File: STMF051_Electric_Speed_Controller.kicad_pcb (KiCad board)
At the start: 4 copper layers, 46 x 47 mm, 166 parts, among them J1 Conn_01x03_Pin, J2 Conn_01x03_Pin, J3 Conn_01x03_Pin, J4 Conn_01x03_Pin, J5 Conn_01x03_Pin, J6 Conn_01x03_Pin, Q1 TPH3R704PL,L1Q, Q10 TPH3R704PL,L1Q, Q11 TPH3R704PL,L1Q, Q12 TPH3R704PL,L1Q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

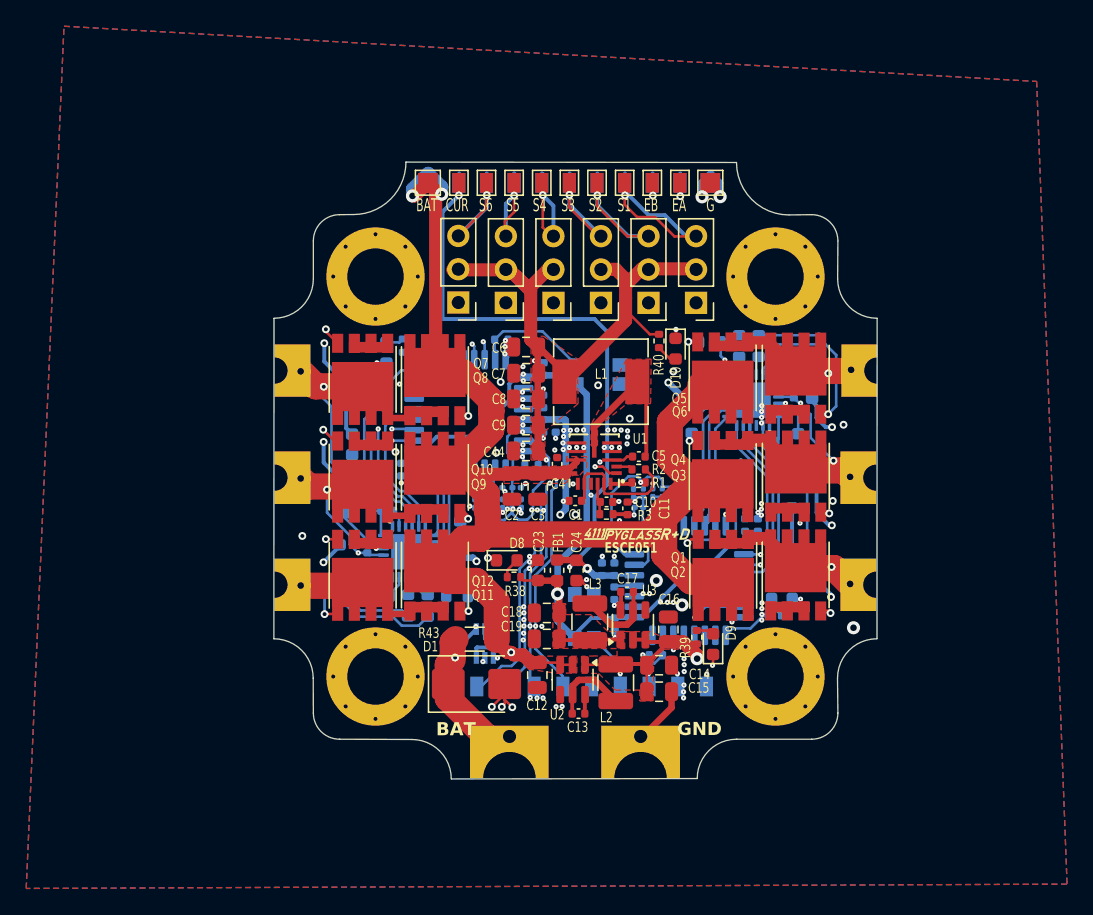
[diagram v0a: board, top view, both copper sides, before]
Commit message: remove blind vias
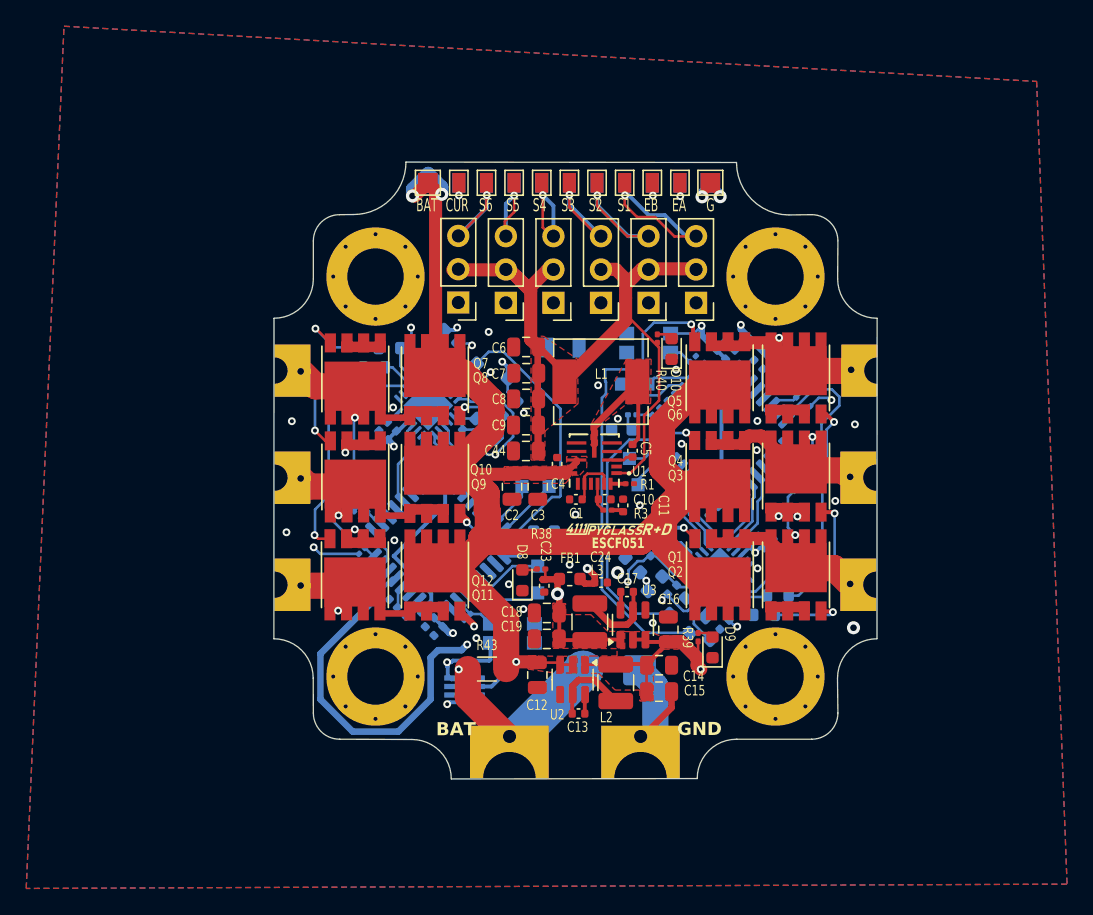
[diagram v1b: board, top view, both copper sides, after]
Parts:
- removed the G*** at (100.7, 91.0)
- removed R2: 22k0, Resistor_SMD:R_0402_1005Metric
- C23, C24: footprint Capacitor_SMD:C_0603_1608Metric -> Capacitor_SMD:C_0402_1005Metric
- D1: moved to B.Cu
- R1, R21, R22, R3, R38, R39, R4, R40, R41, R42, R5: footprint Resistor_SMD:R_0402_1005Metric -> ProjectLibrary:R_0201_0603Metric
- TP10, TP11, TP3, TP4, TP8, TP9: footprint ProjectLibrary:TestPoint_Pad_1.0x1.5mm -> TestPoint:TestPoint_Pad_1.0x1.0mm
- TP5: renamed from TP6; footprint ProjectLibrary:TestPoint_Pad_1.0x1.5mm -> TestPoint:TestPoint_Pad_1.0x1.0mm
- TP6: renamed from TP7; footprint ProjectLibrary:TestPoint_Pad_1.0x1.5mm -> TestPoint:TestPoint_Pad_1.0x1.0mm
- moved TP7 26.9 mm to (97.8, 91.2)
- moved TP12 25.8 mm to (100.3, 91.2)
- moved TP4 23.2 mm to (105.5, 94.0), turned to 0 degrees
- moved TP3 23.2 mm to (103.5, 94.0), turned to 0 degrees
- moved R5 22.8 mm to (109.0, 92.0), turned to 45 degrees
- moved C21 22.4 mm to (111.8, 91.7), turned to 45 degrees
- moved R19 21.6 mm to (109.3, 112.3), turned to 45 degrees
- moved D4 21.5 mm to (109.7, 114.0), turned to -135 degrees
- moved SW1 21.4 mm to (105.6, 90.8), turned to 180 degrees
- moved R21 21.3 mm to (91.8, 111.7), turned to -135 degrees
- moved SW2 20.8 mm to (95.2, 113.0)
- moved C25 20.6 mm to (114.0, 92.5), turned to -45 degrees
- moved C27 20.4 mm to (115.9, 93.1), turned to -45 degrees
- moved R15 19.8 mm to (114.4, 111.5)
- moved C32 19.4 mm to (111.4, 112.3), turned to 45 degrees
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- renumbered TP5 to TP7
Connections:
- net Net-(Q1-Pad4) renamed /FET Driver/HOGate01_A
- net Net-(Q10-Pad4) renamed /FET Driver/LOGate02_B
- net Net-(Q11-Pad4) renamed /FET Driver/HOGate03_B
- net Net-(Q12-Pad4) renamed /FET Driver/LOGate03_B
- net Net-(Q2-Pad4) renamed /FET Driver/LOGate01_A
- net Net-(Q3-Pad4) renamed /FET Driver/HOGate02_A
- net Net-(Q4-Pad4) renamed /FET Driver/LOGate02_A
- net Net-(Q5-Pad4) renamed /FET Driver/HOGate03_A
- net Net-(Q6-Pad4) renamed /FET Driver/LOGate03_A
- net Net-(Q7-Pad4) renamed /FET Driver/HOGate01_B
- net Net-(Q8-Pad4) renamed /FET Driver/LOGate01_B
- net Net-(Q9-Pad4) renamed /FET Driver/HOGate02_B
- SW1 pad 1: /MCU/BOOT0_A -> +3.3V
- SW1 pad 2: +3.3V -> /MCU/BOOT0_A
- U1 pad 2: Net-(U1-*RESET) -> unconnected-(U1-*RESET-Pad2)
- U4 pad 18: HIN1_A -> HIN3_A
- U4 pad 20: HIN3_A -> HIN1_A
- U6 pad 18: HIN1_B -> HIN3_B
- U6 pad 20: HIN3_B -> HIN1_B
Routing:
- net +5V: track 187.2 -> 122.6 mm, vias 9 -> 6
- net +3.3VA: track 22.1 -> 77.0 mm, vias 2 -> 3
- net /FET Driver/HOGate03_A: track 1.81 -> 36.3 mm
- net /FET Driver/HOGate03_B: track 1.82 -> 30.1 mm, vias 1 -> 2
- net RX1_B: track 32.2 -> 5.90 mm, vias 2 -> 0
- net SWDIO_B: track 29.5 -> 3.65 mm, vias 2 -> 0
- net GND: track 44.2 -> 18.7 mm, vias 147 -> 30
- net TX1_B: track 31.3 -> 5.87 mm, vias 2 -> 0
- net SWCLK_B: track 29.8 -> 4.93 mm, vias 2 -> 0
- net PHASE1_A: track 34.6 -> 58.7 mm, vias 3 -> 2
- net PWM2: track 30.5 -> 54.5 mm
- net /FET Driver/HOGate02_B: track 1.49 -> 25.4 mm
- net /FET Driver/HOGate02_A: track 1.32 -> 23.1 mm
- net +3.3V: track 79.3 -> 96.3 mm, vias 2 -> 4
- net /FET Driver/LOGate01_A: track 22.3 -> 5.43 mm, vias 2 -> 1
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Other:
- board text removed: "ESCF051 mgi 07/24"
- board text removed: "RX1A"
- board text removed: "RX1B"
- board text removed: "SCA"
- board text removed: "SCB"
- board text removed: "SDA"
- board text removed: "SDB"
- board text removed: "TX1A"
- board text removed: "TX1B"
